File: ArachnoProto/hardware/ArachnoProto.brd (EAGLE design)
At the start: 59.1 x 64.8 mm, 22 parts, among them J1 PINHEAD-17-REV, J2 PINHEAD-17-REV

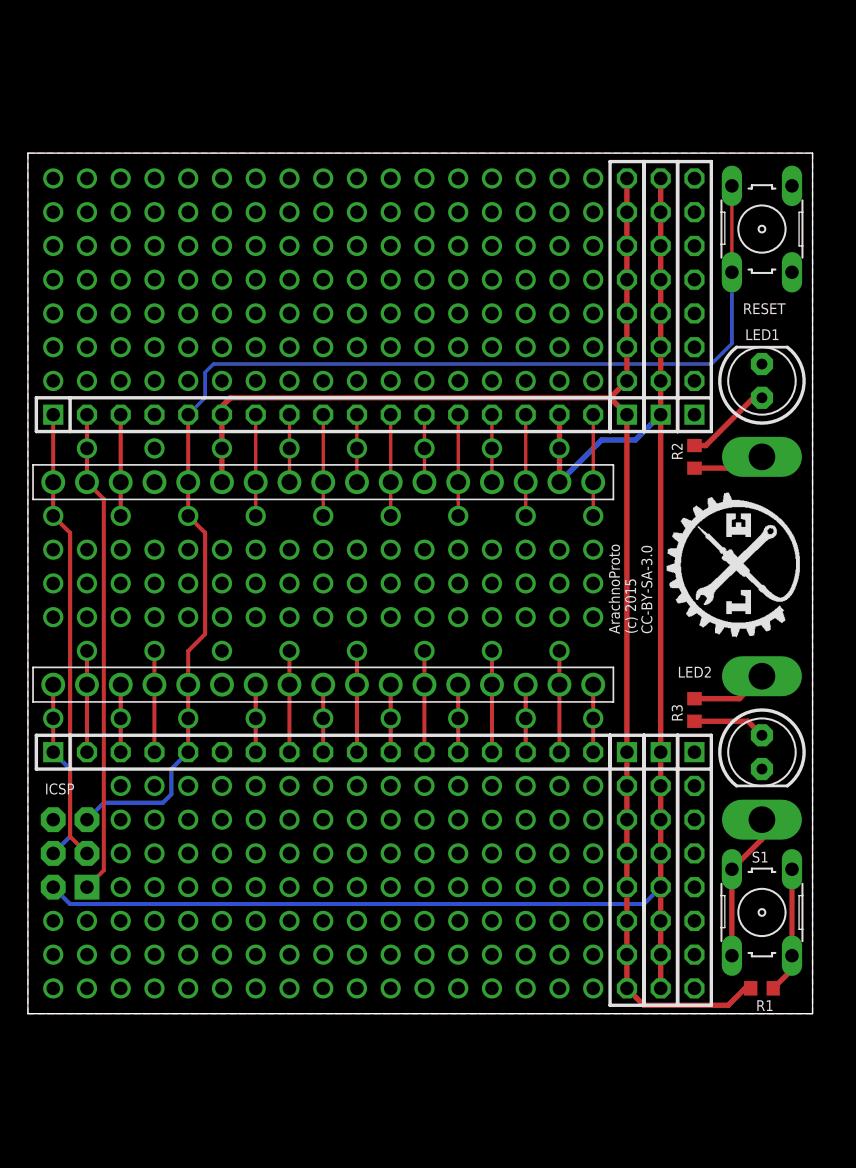
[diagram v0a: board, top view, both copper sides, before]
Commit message: -- Added mounting pads on the board -- Made reset button an independent button -- Changed all components to SMD
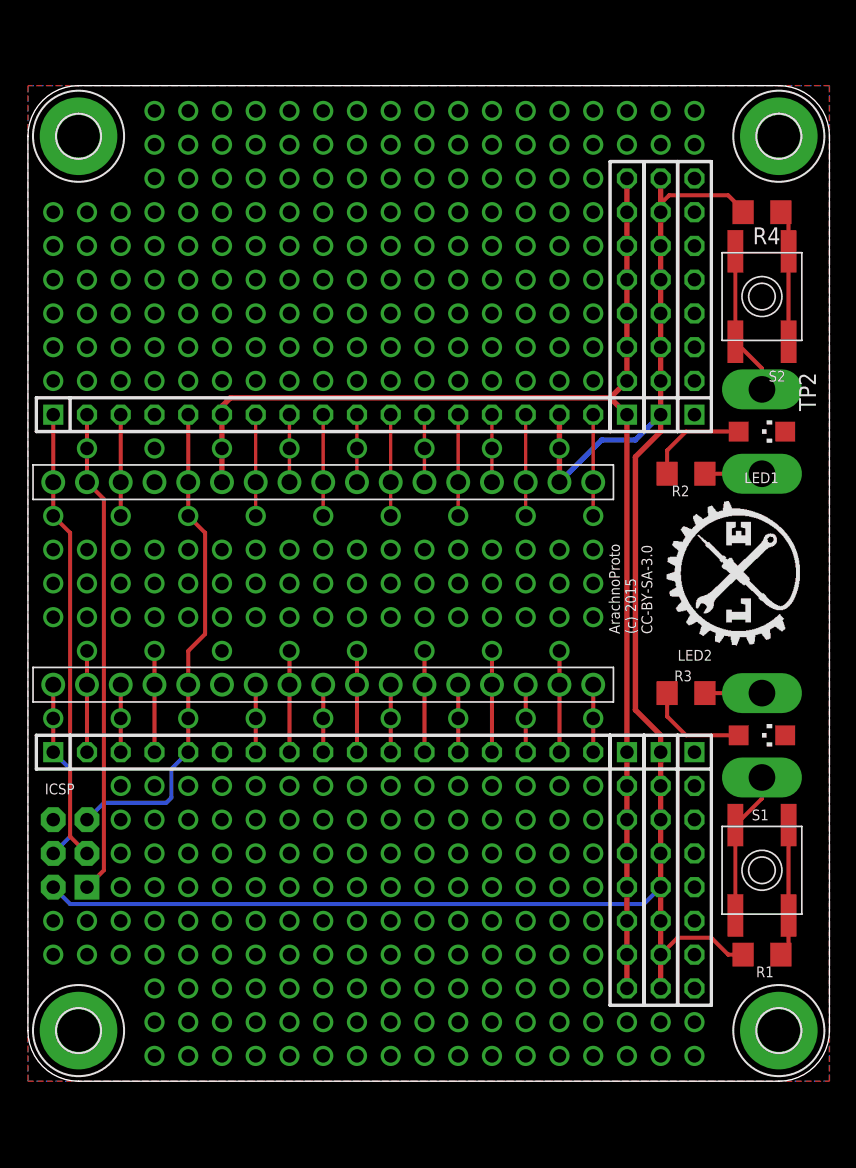
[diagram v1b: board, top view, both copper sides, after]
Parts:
- removed RESET: (no value), switch-omron:B3F-10XX
- added H1, H2, H3, H4: MOUNT-PAD-ROUND3.2, holes:3,2-PAD
- added R4: 1K, resistor:R1206
- added S2: EVQQ2, adafruit:EVQ-Q2
- added TP2: TPSQPAD1-20Y, test-fixtures:P1-20Y
- LED1, LED2: device adafruit:LED5MM -> led:CHIPLED_1206
- R1, R2, R3: device resistor:R0603 -> resistor:R1206
- S1: value (none) -> EVQQ2; device switch-omron:B3F-10XX -> adafruit:EVQ-Q2
- moved LED1 3.81 mm to (55.2, 44.5), turned to 270 degrees
- moved S1 3.17 mm to (55.2, 11.4)
- moved TP1 3.17 mm to (55.2, 18.4)
- moved R1 2.54 mm to (55.2, 5.08)
- moved R2 1.42 mm to (49.5, 41.3), turned to 0 degrees
- moved R3 1.42 mm to (49.5, 24.8), turned to 0 degrees
- moved LED1-PT 1.27 mm to (55.2, 41.3)
- moved LED2 1.27 mm to (55.2, 21.6)
- moved TP3 1.27 mm to (55.2, 24.8)
- moved U$1 0.63 mm to (58.4, 27.9)
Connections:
- new net N$69: R4.1, S2.B, S2.B'
- new net N$70: S2.A, S2.A', TP2.TP
- net +3V3: now also R1.2, R4.2
- net +5V: no longer R1.2
- net GND: now also H1.B3,2, H2.B3,2, H3.B3,2, H4.B3,2, LED1.C, LED2.C; no longer LED1.K, LED2.K, RESET.1, RESET.2
- net N$7: now also S1.A, S1.A'; no longer S1.3, S1.4
- net N$8: now also S1.B, S1.B'; no longer S1.1, S1.2
- net RESET: no longer RESET.3, RESET.4
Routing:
- net RESET: track 93.4 -> 37.4 mm
- net +3V3: track 122.5 -> 138.4 mm
- net N$70: track 0.00 -> 11.3 mm
- net +5V: track 107.6 -> 97.2 mm
- net N$69: track 0.00 -> 9.99 mm
- net N$3: track 5.52 -> 7.73 mm
- net N$6: track 5.78 -> 4.29 mm
- net N$1: track 6.57 -> 7.73 mm
- net N$5: track 5.43 -> 4.29 mm
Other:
- board size 59.1 x 64.8 mm -> 60.3 x 74.9 mm

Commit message: Sometimes eagle is silly...
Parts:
- moved H3 4.45 mm to (56.5, 71.1)
- moved H4 4.45 mm to (3.81, 71.1)
- moved H1 4.45 mm to (56.5, 3.81)
- moved H2 4.45 mm to (3.81, 3.81)
- moved ICSP 4.45 mm to (3.17, 17.1)
- moved J1 4.45 mm to (22.2, 29.8)
- moved J2 4.45 mm to (22.2, 45.1)
- moved JP1 4.45 mm to (22.2, 24.8)
- moved JP2 4.45 mm to (22.2, 50.2)
- moved JP20 4.45 mm to (45.1, 59.1)
- moved JP21 4.45 mm to (45.1, 15.9)
- moved JP22 4.45 mm to (47.6, 59.1)
- moved JP23 4.45 mm to (50.2, 15.9)
- moved JP24 4.45 mm to (50.2, 59.1)
- moved JP25 4.45 mm to (47.6, 15.9)
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
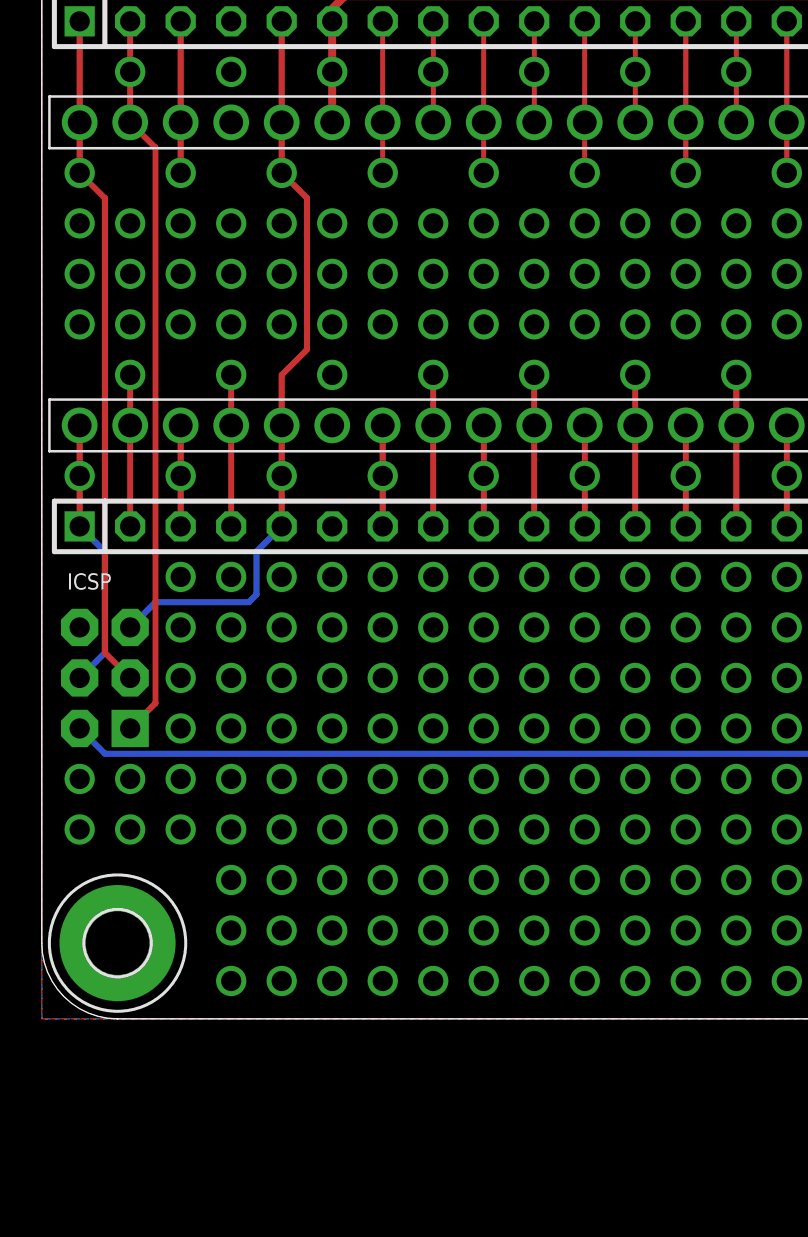
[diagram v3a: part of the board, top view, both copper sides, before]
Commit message: Modified ArachnoProto to work with the ArachnioDue.
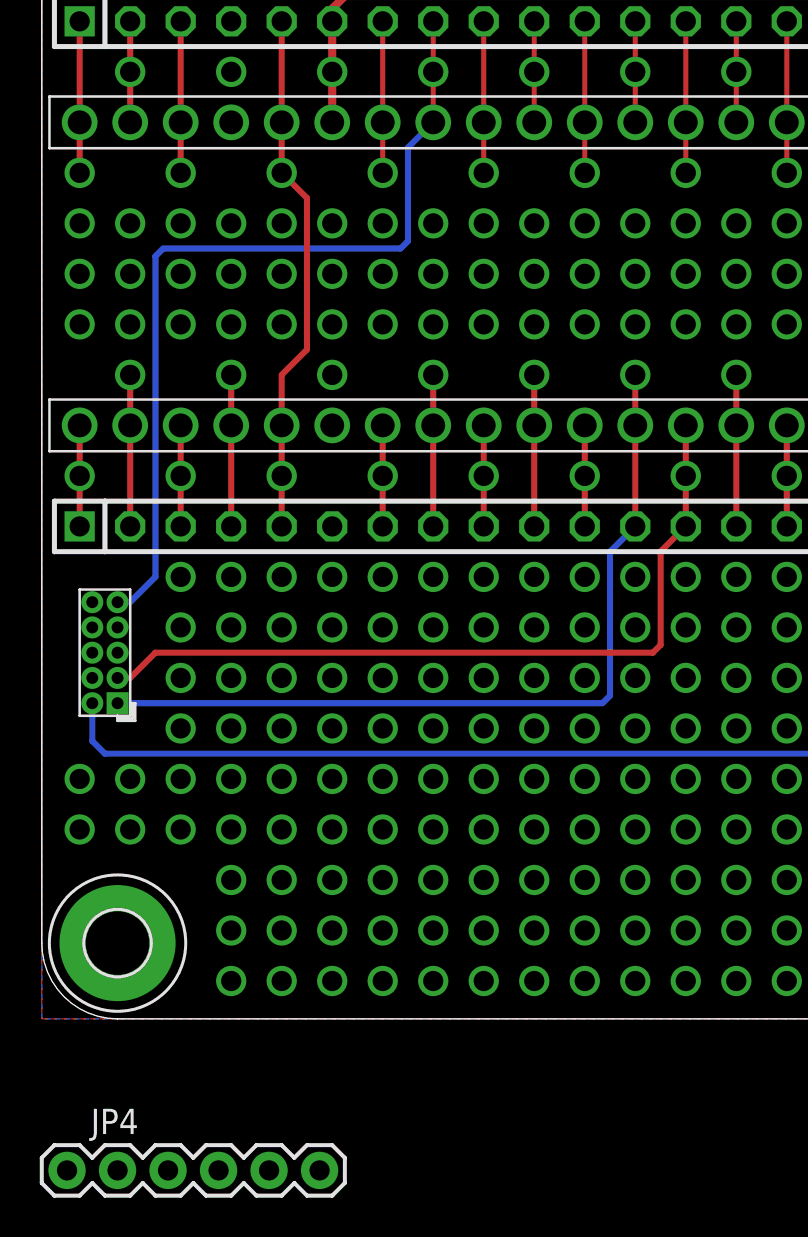
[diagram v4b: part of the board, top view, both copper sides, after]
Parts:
- removed ICSP: AVR_SPI_PRG_6NS, SparkFun-Connectors:2X3-NS
- added JP3: (no value), atmel-d21:PINHEAD_2X05_127
- added JP4: FTDI_BASICPTH, SparkFun-Connectors:FTDI_BASIC
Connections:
- removed net D7: J1.12, J1.29, JP1.12
- removed net IO8: J1.13, J1.30, JP1.13
- new net D7/SWDIO: J1.12, J1.29, JP1.12, JP3.1
- new net IO8/SWCLK: J1.13, J1.30, JP1.13, JP3.3
- new net N$354: JP4.RXI
- new net N$355: JP4.TXO
- net +3V3: now also JP3.2, JP4.VCC; no longer ICSP.2
- net ESP_RST: now also JP3.9
- net GND: now also JP3.4, JP3.6, JP4.GND; no longer ICSP.6
- net MISO: no longer ICSP.1
- net MOSI: no longer ICSP.4
- net RESET: no longer ICSP.5
- net SCK: no longer ICSP.3
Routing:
- net D7/SWDIO: track 0.00 -> 41.6 mm
- net IO8/SWCLK: track 0.00 -> 39.6 mm
- net ESP_RST: track 5.08 -> 43.2 mm
- net MISO: track 36.6 -> 5.08 mm
- net SCK: track 34.1 -> 7.62 mm
- net RESET: track 37.4 -> 26.5 mm
- net MOSI: track 13.8 -> 5.08 mm
- net D7: track 7.62 -> 0.00 mm
- net IO8: track 5.08 -> 0.00 mm
- net +3V3: track 138.4 -> 139.4 mm
